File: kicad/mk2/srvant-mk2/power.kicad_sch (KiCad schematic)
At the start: 70 parts, among them J12 Screw_Terminal_01x02, J2 Conn_01x02, Q1 DMP3013SFV-7, U1 AP63205WU, U15 TLV62585DRLR, U2 AP64501SP-13, U3 74AHC1G32, U4 INA219AxDCN, U9 RT9742SNGV

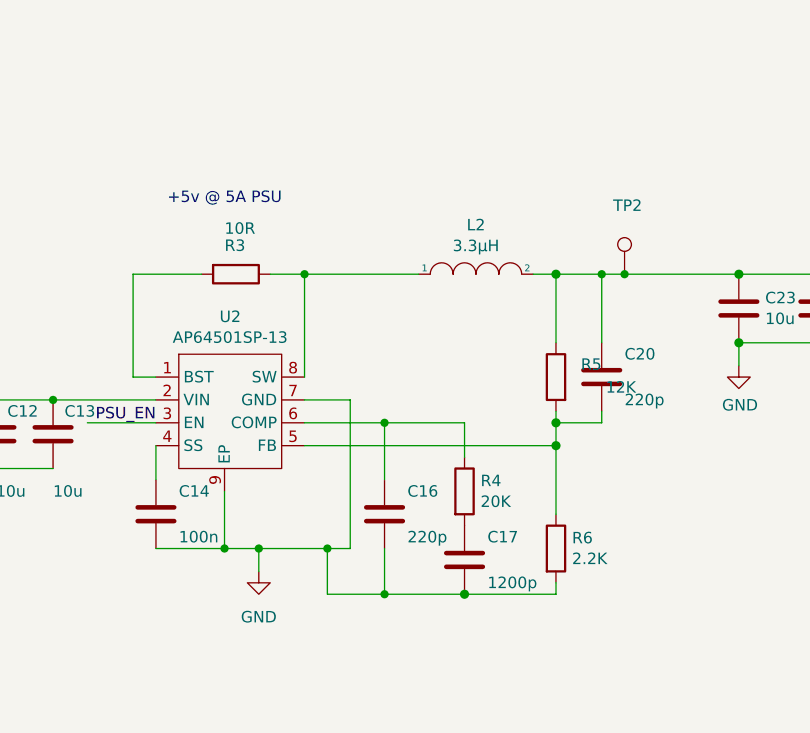
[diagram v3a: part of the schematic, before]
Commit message: Fixes after manufacturing
* Change footprint for the VIN capacitors. 10uf was supposed to be 0804
  not 0402. That required repositioning of both power converters.
* Fix PWR_EN pin override (2.54mm instead of 1.0)
* Change resistor values in voltage divider of AP64501SP. Values taken
  from RPI carrier board produce wrong voltage (~3.6v instead of 5v).
* Add silkscreen labels around the LEDs.
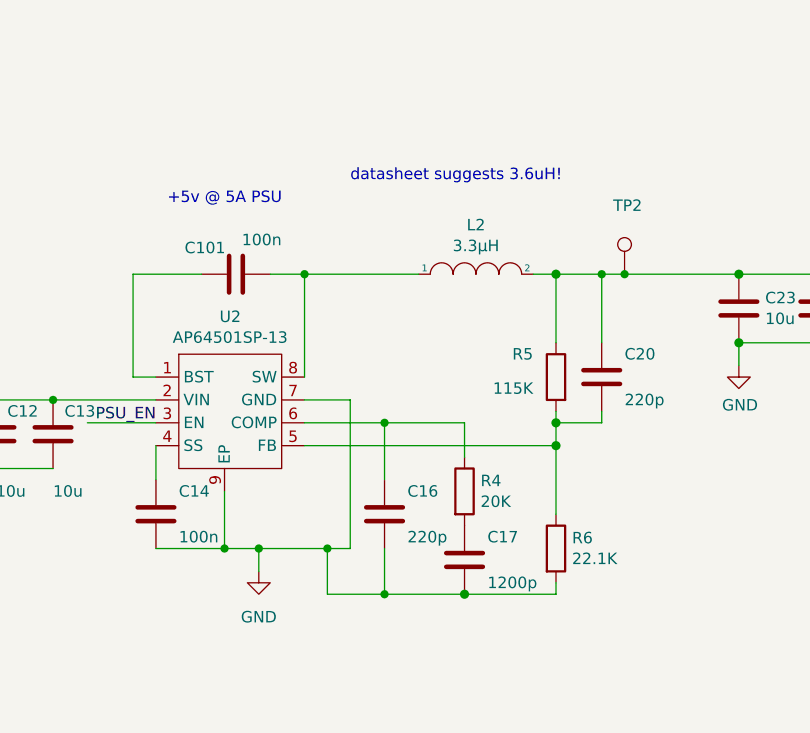
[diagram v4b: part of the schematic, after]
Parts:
- removed R3: 10R, Resistor_SMD:R_0402_1005Metric, symbol Device:R
- added C101: 100n, Capacitor_SMD:C_0402_1005Metric, symbol Device:C
- C10, C11, C12, C13, C3, C4, C5, C6, C7, C8, C9: footprint Capacitor_SMD:C_0402_1005Metric -> Capacitor_SMD:C_0805_2012Metric
- J2: footprint Connector_PinHeader_1.00mm:PinHeader_1x02_P1.00mm_Vertical -> Connector_PinHeader_2.54mm:PinHeader_1x02_P2.54mm_Vertical
- R5: value 12K -> 115K; Part Description Resistor 12K M1005 1% 63mW -> (none); farnell# 9239367 -> (none); manf# MCR01MZPF1202 -> (none)
- R6: value 2.2K -> 22.1K; Field8 120889581 -> (none); Part Description Resistor 2.2K M1005 1% 63mW -> (none); farnell# 9239278 -> (none); manf# RK73G1ETQTP2201D -> (none)
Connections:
- net at L2.1, U2.8 (SW): now also C101.2
- net at U2.1 (BST): now also C101.1
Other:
- note added: "datasheet suggests 3.6uH!"
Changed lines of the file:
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@@
     (effects (font (size 1.27 1.27)) (justify left bottom))
   )
+  (text "datasheet suggests 3.6uH!" (at 189.23 87.63 0)
+    (effects (font (size 1.27 1.27)) (justify left bottom))
+  )
   (text "3.3v @ 3A PSU For PCIE\n\n" (at 222.123 227.457 0)
     (effects (font (size 1.27 1.27) (thickness 0.254) bold) (justify left bottom))
@@
       (effects (font (size 1.27 1.27)) (justify left))
     )
-    (property "Footprint" "Capacitor_SMD:C_0402_1005Metric" (at 138.1252 119.38 0)
+    (property "Footprint" "Capacitor_SMD:C_0805_2012Metric" (at 138.1252 119.38 0)
       (effects (font (size 1.27 1.27)) hide)
     )
@@
     )
   )
-  (symbol (lib_id "Device:R") (at 176.53 97.79 270) (unit 1)
-    (in_bom yes) (on_board yes) (dnp no)
-    (property "Reference" "R3" (at 175.26 94.615 90)
-      (effects (font (size 1.27 1.27)) (justify left))
-    )
-    (property "Value" "10R" (at 175.26 92.71 90)
-      (effects (font (size 1.27 1.27)) (justify left))
-    )
-    (property "Footprint" "Resistor_SMD:R_0402_1005Metric" (at 176.53 96.012 90)
-      (effects (font (size 1.27 1.27)) hide)
-    )
-    (property "Datasheet" "https://fscdn.rohm.com/en/products/databook/datasheet/passive/resistor/chip_resistor/mcr-e.pdf" (at 176.53 97.79 0)
-      (effects (font (size 1.27 1.27)) hide)
-    )
-    (property "Part Description" "Resistor 10R M1005 1% 63mW" (at 176.53 97.79 0)
-      (effects (font (size 1.27 1.27)) hide)
-    )
-    (property "manf#" "RC0402FR-0710RL" (at 176.53 97.79 0)
-      (effects (font (size 1.27 1.27)) hide)
-    )
-    (property "digikey#" "" (at 176.53 97.79 0)
-      (effects (font (size 1.27 1.27)) hide)
-    )
-    (property "mouser#" "" (at 176.53 97.79 0)
-      (effects (font (size 1.27 1.27)) hide)
-    )
-    (property "farnell#" "9238999" (at 176.53 97.79 0)
-      (effects (font (size 1.27 1.27)) hide)
-    )
-    (property "rs#" "" (at 176.53 97.79 0)
-      (effects (font (size 1.27 1.27)) hide)
-    )
-    (pin "1")
-    (pin "2")
-    (instances
-      (project "srvant-mk2"
-        (path "/1859a578-b791-4142-bdf4-fda494df1146/c300a602-5caa-44c4-bd60-e0bac469451e"
-          (reference "R3") (unit 1)
-        )
-      )
-      (project "srvant"
-        (path "/556fa623-1b37-4e79-bae4-da8a8b5c51e2/77f0feb9-dd36-46a2-a219-577028a19cb5"
-          (reference "R2") (unit 1)
-        )
-      )
-    )
-  )
   (symbol (lib_id "Device:R") (at 212.09 109.22 0) (mirror y) (unit 1)
     (in_bom yes) (on_board yes) (dnp no)
-    (property "Reference" "R5" (at 217.17 107.823 0)
+    (property "Reference" "R5" (at 209.55 106.68 0)
       (effects (font (size 1.27 1.27)) (justify left))
     )
-    (property "Value" "12K" (at 220.98 110.363 0)
+    (property "Value" "115K" (at 209.55 110.49 0)
       (effects (font (size 1.27 1.27)) (justify left))
     )
@@
       (effects (font (size 1.27 1.27)) hide)
     )
-    (property "Datasheet" "https://fscdn.rohm.com/en/products/databook/datasheet/passive/resistor/chip_resistor/mcr-e.pdf" (at 212.09 109.22 0)
+    (property "Datasheet" "" (at 212.09 109.22 0)
       (effects (font (size 1.27 1.27)) hide)
     )
-    (property "Part Description" "Resistor 12K M1005 1% 63mW" (at 212.09 109.22 0)
+    (property "Part Description" "" (at 212.09 109.22 0)
       (effects (font (size 1.27 1.27)) hide)
     )
-    (property "manf#" "MCR01MZPF1202" (at 212.09 109.22 0)
+    (property "manf#" "" (at 212.09 109.22 0)
       (effects (font (size 1.27 1.27)) hide)
     )
@@
       (effects (font (size 1.27 1.27)) hide)
     )
-    (property "farnell#" "9239367" (at 212.09 109.22 0)
+    (property "farnell#" "" (at 212.09 109.22 0)
       (effects (font (size 1.27 1.27)) hide)
     )
@@
       (effects (font (size 1.27 1.27)) (justify left))
     )
-    (property "Value" "2.2K" (at 213.868 129.413 0)
+    (property "Value" "22.1K" (at 213.868 129.413 0)
       (effects (font (size 1.27 1.27)) (justify left))
     )
@@
       (effects (font (size 1.27 1.27)) hide)
     )
-    (property "Datasheet" "https://fscdn.rohm.com/en/products/databook/datasheet/passive/resistor/chip_resistor/mcr-e.pdf" (at 212.09 128.27 0)
+    (property "Datasheet" "" (at 212.09 128.27 0)
       (effects (font (size 1.27 1.27)) hide)
     )
-    (property "Part Description" "Resistor 2.2K M1005 1% 63mW" (at 212.09 128.27 0)
+    (property "Part Description" "" (at 212.09 128.27 0)
       (effects (font (size 1.27 1.27)) hide)
     )
-    (property "Field8" "120889581" (at 212.09 128.27 0)
+    (property "Field8" "" (at 212.09 128.27 0)
       (effects (font (size 1.27 1.27)) hide)
     )
-    (property "manf#" "RK73G1ETQTP2201D" (at 212.09 128.27 0)
+    (property "manf#" "" (at 212.09 128.27 0)
       (effects (font (size 1.27 1.27)) hide)
     )
@@
       (effects (font (size 1.27 1.27)) hide)
     )
-    (property "farnell#" "9239278" (at 212.09 128.27 0)
+    (property "farnell#" "" (at 212.09 128.27 0)
       (effects (font (size 1.27 1.27)) hide)
     )
@@
       (effects (font (size 1.27 1.27)) (justify left))
     )
-    (property "Footprint" "Capacitor_SMD:C_0402_1005Metric" (at 157.1752 119.38 0)
+    (property "Footprint" "Capacitor_SMD:C_0805_2012Metric" (at 157.1752 119.38 0)
       (effects (font (size 1.27 1.27)) hide)
     )
@@
     )
   )
+  (symbol (lib_id "Device:C") (at 176.53 97.79 90) (unit 1)
+    (in_bom yes) (on_board yes) (dnp no)
+    (property "Reference" "C101" (at 175.3616 94.869 90)
+      (effects (font (size 1.27 1.27)) (justify left))
+    )
+    (property "Value" "100n" (at 181.61 93.98 90)
+      (effects (font (size 1.27 1.27)) (justify left))
+    )
+    (property "Footprint" "Capacitor_SMD:C_0402_1005Metric" (at 180.34 96.8248 0)
+      (effects (font (size 1.27 1.27)) hide)
+    )
+    (property "Datasheet" "SRN4018-4R7M" (at 176.53 97.79 0)
+      (effects (font (size 1.27 1.27)) hide)
+    )
+    (property "Field4" "Farnell" (at 176.53 97.79 0)
+      (effects (font (size 1.27 1.27)) hide)
+    )
+    (property "Field5" "2611911" (at 176.53 97.79 0)
+      (effects (font (size 1.27 1.27)) hide)
+    )
+    (property "Field6" "RM EMK105 B7104KV-F" (at 176.53 97.79 0)
+      (effects (font (size 1.27 1.27)) hide)
+    )
+    (property "Field7" "TAIYO YUDEN EUROPE GMBH" (at 176.53 97.79 0)
+      (effects (font (size 1.27 1.27)) hide)
+    )
+    (property "Part Description" "0.1uF 10% 16V Ceramic Capacitor X7R 0402 (1005 Metric)" (at 176.53 97.79 0)
+      (effects (font (size 1.27 1.27)) hide)
+    )
+    (property "Field8" "110091611" (at 176.53 97.79 0)
+      (effects (font (size 1.27 1.27)) hide)
+    )
+    (pin "1")
+    (pin "2")
+    (instances
+      (project "srvant-mk2"
+        (path "/1859a578-b791-4142-bdf4-fda494df1146/c300a602-5caa-44c4-bd60-e0bac469451e"
+          (reference "C101") (unit 1)
+        )
+      )
+    )
+  )
   (symbol (lib_id "Device:C") (at 149.86 115.57 0) (unit 1)
     (in_bom yes) (on_board yes) (dnp no) (fields_autoplaced)
@@
       (effects (font (size 1.27 1.27)) (justify left))
     )
-    (property "Footprint" "Capacitor_SMD:C_0402_1005Metric" (at 150.8252 119.38 0)
+    (property "Footprint" "Capacitor_SMD:C_0805_2012Metric" (at 150.8252 119.38 0)
       (effects (font (size 1.27 1.27)) hide)
     )
@@
       (effects (font (size 1.27 1.27)) (justify left))
     )
-    (property "Footprint" "Capacitor_SMD:C_0402_1005Metric" (at 131.7752 175.26 0)
+    (property "Footprint" "Capacitor_SMD:C_0805_2012Metric" (at 131.7752 175.26 0)
       (effects (font (size 1.27 1.27)) hide)
     )
@@
       (effects (font (size 1.27 1.27)) (justify left))
     )
-    (property "Footprint" "Capacitor_SMD:C_0402_1005Metric" (at 125.4252 175.26 0)
+    (property "Footprint" "Capacitor_SMD:C_0805_2012Metric" (at 125.4252 175.26 0)
       (effects (font (size 1.27 1.27)) hide)
     )
@@
       (effects (font (size 1.27 1.27)) (justify left))
     )
-    (property "Footprint" "Capacitor_SMD:C_0402_1005Metric" (at 125.4252 119.38 0)
+    (property "Footprint" "Capacitor_SMD:C_0805_2012Metric" (at 125.4252 119.38 0)
       (effects (font (size 1.27 1.27)) hide)
     )
@@
       (effects (font (size 1.27 1.27)) (justify left))
     )
-    (property "Footprint" "Capacitor_SMD:C_0402_1005Metric" (at 144.4752 119.38 0)
+    (property "Footprint" "Capacitor_SMD:C_0805_2012Metric" (at 144.4752 119.38 0)
       (effects (font (size 1.27 1.27)) hide)
     )
@@
       (effects (font (size 1.27 1.27)))
     )
-    (property "Footprint" "Connector_PinHeader_1.00mm:PinHeader_1x02_P1.00mm_Vertical" (at 313.69 139.7 0)
+    (property "Footprint" "Connector_PinHeader_2.54mm:PinHeader_1x02_P2.54mm_Vertical" (at 313.69 139.7 0)
       (effects (font (size 1.27 1.27)) hide)
     )
@@
       (effects (font (size 1.27 1.27)) (justify left))
     )
-    (property "Footprint" "Capacitor_SMD:C_0402_1005Metric" (at 138.1252 175.26 0)
+    (property "Footprint" "Capacitor_SMD:C_0805_2012Metric" (at 138.1252 175.26 0)
       (effects (font (size 1.27 1.27)) hide)
     )
@@
       (effects (font (size 1.27 1.27)) (justify left))
     )
-    (property "Footprint" "Capacitor_SMD:C_0402_1005Metric" (at 131.7752 119.38 0)
+    (property "Footprint" "Capacitor_SMD:C_0805_2012Metric" (at 131.7752 119.38 0)
       (effects (font (size 1.27 1.27)) hide)
     )
@@
       (effects (font (size 1.27 1.27)) (justify left))
     )
-    (property "Footprint" "Capacitor_SMD:C_0402_1005Metric" (at 119.0752 175.26 0)
+    (property "Footprint" "Capacitor_SMD:C_0805_2012Metric" (at 119.0752 175.26 0)
       (effects (font (size 1.27 1.27)) hide)
     )
@@
       (effects (font (size 1.27 1.27)) (justify left))
     )
-    (property "Footprint" "Capacitor_SMD:C_0402_1005Metric" (at 97.4852 130.81 0)
+    (property "Footprint" "Capacitor_SMD:C_0805_2012Metric" (at 97.4852 130.81 0)
       (effects (font (size 1.27 1.27)) hide)
     )

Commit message: redesign for the next version
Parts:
- removed R54: 100K, Resistor_SMD:R_0402_1005Metric, symbol Device:R
- removed TP6: VIN, TestPoint:TestPoint_Pad_D1.0mm, symbol ARJM11:TestPoint
- removed U15: TLV62585DRLR, TLV62585DRLR:DRL0006A, symbol TLV62585DRLR:TLV62585DRLR
- added C103: 22uF, Capacitor_SMD:C_0402_1005Metric, symbol Device:C
- added C106, C107, C108, C109, C110, C116, C117, C118, C119, C121: 10u, Capacitor_SMD:C_0805_2012Metric, symbol Device:C
- added C111, C112: 100n, Capacitor_SMD:C_0402_1005Metric, symbol Device:C
- added C113, C115: 220p, Capacitor_SMD:C_0402_1005Metric, symbol Device:C
- added C114: 1200p, Capacitor_SMD:C_0402_1005Metric, symbol Device:C
- added C120: 100u, Capacitor_Tantalum_SMD:CP_EIA-7343-31_Kemet-D, symbol Device:CP
- added J1: 1724480004, footprints:CONN04_1724480004_MOL, symbol molex4pin:1724480004
- added L4: 3.3µH, Inductor_SMD:L_Bourns_SRN6045TA, symbol pspice:INDUCTOR
- added R16: 10R, Resistor_SMD:R_0402_1005Metric, symbol Device:R
- added R3: 100K, Resistor_SMD:R_0402_1005Metric, symbol Device:R
- added R58: 30K, Resistor_SMD:R_0402_1005Metric, symbol Device:R
- added R62: 22R, Resistor_SMD:R_0402_1005Metric, symbol Device:R
- added R63: 12K, Resistor_SMD:R_0402_1005Metric, symbol Device:R
- added R64: 47K, Resistor_SMD:R_0402_1005Metric, symbol Device:R
- added R69: 15K, Resistor_SMD:R_0402_1005Metric, symbol Device:R
- added TP23: +5v HOST, TestPoint:TestPoint_Pad_2.0x2.0mm, symbol Connector:TestPoint
- added U16: TPS563203, Package_TO_SOT_SMD:SOT-563, symbol Regulator_Switching:TPS563203
- added U26: AP64501SP-13, Package_SO:SOIC-8-1EP_3.9x4.9mm_P1.27mm_EP2.95x4.9mm_Mask2.71x3.4mm_ThermalVias, symbol CM4IO:AP64351
- C100, C76, C78: value 10u -> 100n; footprint Capacitor_SMD:C_0805_2012Metric -> Capacitor_SMD:C_0402_1005Metric; Field4 Digikey -> (none); Field5 490-10505-1-ND -> (none); Field6 GRM21BC8YA106KE11L -> (none); Field7 Murata -> (none); Field8 111893011 -> (none); Part Description 10uF 10% 10V Ceramic Capacitor X7R 0805 (2012 Metric) -> 0.1uF 10% 16V Ceramic Capacitor X7R 0402 (1005 Metric); digikey# 490-14381-1-ND -> EMK105B7104KV-F; farnell# (none) -> 2611911; manf# GRM21BR71A106KA73L -> GRM155R71C104KA88; mouser# (none) -> 963-EMK105B7104KV-F; now not fitted; now left out of the parts list
- C101: value 100n -> 22uF; Field4 Farnell -> (none); Field5 2611911 -> (none); Field6 RM EMK105 B7104KV-F -> (none); Field7 TAIYO YUDEN EUROPE GMBH -> (none); Field8 110091611 -> (none); Part Description 0.1uF 10% 16V Ceramic Capacitor X7R 0402 (1005 Metric) -> (none); farnell# (none) -> 2611911; now not fitted; now left out of the parts list
- C16, C20: now not fitted
- C69: value 10u -> 100n; footprint Capacitor_SMD:C_0805_2012Metric -> Capacitor_SMD:C_0402_1005Metric; Field4 Digikey -> Farnell; Field5 490-10505-1-ND -> 2611911; Field6 GRM21BC8YA106KE11L -> RM EMK105 B7104KV-F; Field7 Murata -> TAIYO YUDEN EUROPE GMBH; Field8 111893011 -> 110091611; Part Description 10uF 10% 10V Ceramic Capacitor X7R 0805 (2012 Metric) -> 0.1uF 10% 16V Ceramic Capacitor X7R 0402 (1005 Metric); digikey# 490-14381-1-ND -> (none); manf# GRM21BR71A106KA73L -> (none)
- C71: Field4 Digikey -> (none); Field5 490-10505-1-ND -> (none); Field6 GRM21BC8YA106KE11L -> (none); Field7 Murata -> (none); Field8 111893011 -> (none); Part Description 10uF 10% 10V Ceramic Capacitor X7R 0805 (2012 Metric) -> 10uF 10% or 20% 35V Ceramic Capacitor X6S 0805 (2012 Metric); digikey# 490-14381-1-ND -> 490-10505-1-ND; manf# GRM21BR71A106KA73L -> GRM21BC8YA106KE11L; now not fitted; now left out of the parts list
- C80: value 10u -> 22pf; footprint Capacitor_SMD:C_0805_2012Metric -> Capacitor_SMD:C_0402_1005Metric; Field4 Digikey -> (none); Field5 490-10505-1-ND -> (none); Field8 111893011 -> (none); Part Description 10uF 10% 10V Ceramic Capacitor X7R 0805 (2012 Metric) -> (none); digikey# 490-14381-1-ND -> (none); manf# GRM21BR71A106KA73L -> (none); now not fitted; now left out of the parts list
- L3: value 1µH -> 4.7µH; footprint Inductor_SMD:L_Bourns_SRN6045TA -> Inductor_SMD:L_Bourns-SRN4018; Part Description 1µH Semi-Shielded Wirewound Inductor 8A -> 4.7µH Semi-Shielded Wirewound Inductor 1.9A 84mOhm Standard; farnell# 2616885 -> 2329227; manf# SRN6045TA-1R0Y -> SRN4018-4R7M; mouser# (none) -> 652-SRN4018-4R7M; now not fitted; now left out of the parts list
- R10, R9: value 3.3K -> 10K
- R55: value 22K -> 135K; Field4 Farnell -> (none); Field5 9239430 -> (none); Field6 RK73G1ETQTP4702D -> (none); Field7 KOA EUROPE GMBH -> (none); Field8 120892781 -> (none); Part Description Resistor 22K M1005 1% 63mW -> (none); farnell# 9239430 -> (none); manf# RC0402FR-0747KL -> (none); now not fitted; now left out of the parts list
- TP16: footprint TestPoint:TestPoint_Pad_D1.0mm -> TestPoint:TestPoint_Pad_2.0x2.0mm
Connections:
- net +5v_HOST: no longer C69.1, C71.1
- net GND: now also C106.2, C107.2, C108.2, C109.2, C110.2, C112.2, C113.2, C114.2, C116.2, C117.2, C118.2, C119.2, C120.2, C121.2, J1.1, J1.2, R69.2, U26.7 (GND), U26.9 (EP); no longer C100.2, C69.2, C71.2, C76.2, C78.2, C80.2, R55.2
- net SENSE_IN-: now also C71.1, C76.2, C106.1, C107.1, C108.1, C109.1, C110.1, C121.1, R3.1, U16.1 (VIN), U26.2 (VIN), U26.3 (EN)
- net VIN: now also J1.3, J1.4
- net at L2.1, U2.8 (SW): now also R16.2; no longer C101.2
- net at U2.1 (BST): now also C69.1; no longer C101.1
- net at L3.1: now also C78.1, U16.2 (SW)
- net +3.3v_BMC renamed +3v3_AUX
- net +3v3_AUX: now also C100.1, C101.1, C80.1, L3.2, R55.2, C103.1, C115.1, C116.1, C117.1, C118.1, C119.1, C120.1, L4.2, R64.1, TP23.1
- removed net +3.3v_HOST_PCIe: C100.1, C76.1, C78.1, C80.1, L3.2
- net 3V3P_FB: no longer names the net of R55.1
- net 3V3P_FB: now also C80.2, R58.1, U16.6 (FB)
- new net: C113.1, R63.1, U26.6 (COMP)
- new net: C115.2, R64.2, R69.1, U26.5 (FB)
- new net: C111.1, U26.1 (BST)
- new net: C112.1, U26.4 (SS)
- new net: L4.1, R62.2, U26.8 (SW)
- new net: C111.2, R62.1
- new net: R3.2, U16.5 (EN)
- new net: C100.2, C101.2, C103.2, C71.2, C76.1, R58.2, U16.3 (GND)
- new net: C69.2, R16.1
- new net: C78.2, U16.4 (BST)
- new net: C114.1, R63.2
- no-connect marks 1 -> 0
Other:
- note added: "+3.3v @ 3A AUX"
- note added: "12v input"
- note added: "C16 and C20 are `nf` in CM4IO schematic"
- note removed: "3.3v @ 3A PSU For PCIE"
- note removed: "7.5v-26v input"
- note removed: "PCIe power"
- moved on the sheet: C10, C11, C12, C13, C15, C18, C19, C21, C22, C24, C4, C5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

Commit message: v1.5 draft
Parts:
- C72, C73, U9: now not fitted; now left out of the parts list
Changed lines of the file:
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@@
 		(at 351.79 185.42 0)
 		(unit 1)
-		(exclude_from_sim no)
-		(in_bom yes)
-		(on_board yes)
-		(dnp no)
+		(exclude_from_sim yes)
+		(in_bom no)
+		(on_board no)
+		(dnp yes)
 		(property "Reference" "#PWR046"
 			(at 351.79 191.77 0)
@@
 		(at 318.77 181.61 0)
 		(unit 1)
-		(exclude_from_sim no)
-		(in_bom yes)
-		(on_board yes)
-		(dnp no)
+		(exclude_from_sim yes)
+		(in_bom no)
+		(on_board no)
+		(dnp yes)
 		(property "Reference" "C72"
 			(at 321.691 180.4416 0)
@@
 		(at 335.28 181.61 0)
 		(unit 1)
-		(exclude_from_sim no)
-		(in_bom yes)
-		(on_board yes)
-		(dnp no)
+		(exclude_from_sim yes)
+		(in_bom no)
+		(on_board no)
+		(dnp yes)
 		(property "Reference" "U9"
 			(at 337.82 171.069 0)
@@
 		(at 318.77 185.42 0)
 		(unit 1)
-		(exclude_from_sim no)
-		(in_bom yes)
-		(on_board yes)
-		(dnp no)
+		(exclude_from_sim yes)
+		(in_bom no)
+		(on_board no)
+		(dnp yes)
 		(property "Reference" "#PWR042"
 			(at 318.77 191.77 0)
@@
 		(at 351.79 181.61 0)
 		(unit 1)
-		(exclude_from_sim no)
-		(in_bom yes)
-		(on_board yes)
-		(dnp no)
+		(exclude_from_sim yes)
+		(in_bom no)
+		(on_board no)
+		(dnp yes)
 		(property "Reference" "C73"
 			(at 354.711 180.4416 0)
@@
 		(at 330.2 185.42 0)
 		(unit 1)
-		(exclude_from_sim no)
-		(in_bom yes)
-		(on_board yes)
-		(dnp no)
+		(exclude_from_sim yes)
+		(in_bom no)
+		(on_board no)
+		(dnp yes)
 		(property "Reference" "#PWR044"
 			(at 330.2 191.77 0)
